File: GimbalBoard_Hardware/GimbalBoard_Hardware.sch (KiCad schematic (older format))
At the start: 3 parts

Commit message: added zenner diodes
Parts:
- added D1, D2: D_Zener, symbol Device:D_Zener
- gave numbers to parts that had none: 1
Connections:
- wire segments 26 -> 36
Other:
- note added: "Buck Converters"
- note added: "Power Input"
- moved on the sheet: Conn1A, Conn1B, Conn1C

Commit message: added servo indicator sheet and some connection
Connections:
- net labels removed: Servo_1_PWM, Servo_2_PWM, Servo_3_PWM, Servo_4_PWM, Servo_5_PWM, Servo_6_PWM, Servo_7_PWM, Servo_8_PWM
- wire segments 36 -> 37
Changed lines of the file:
@@
 $Descr A4 11693 8268
 encoding utf-8
-Sheet 1 6
+Sheet 1 7
 Title ""
 Date ""
@@
 Wire Wire Line
 	10000 1750 10250 1750
-Text GLabel 6050 4000 0    50   Output ~ 0
+Text GLabel 4850 900  0    50   Output ~ 0
 Servo_1_SW
 Wire Wire Line
-	6050 4000 6200 4000
-Text GLabel 6050 4150 0    50   Output ~ 0
+	4850 900  5000 900
+Text GLabel 4850 1050 0    50   Output ~ 0
 Servo_2_SW
 Wire Wire Line
-	6050 4150 6200 4150
-Text GLabel 6050 4300 0    50   Output ~ 0
+	4850 1050 5000 1050
+Text GLabel 4850 1200 0    50   Output ~ 0
 Servo_3_SW
 Wire Wire Line
-	6050 4300 6200 4300
-Text GLabel 6050 4450 0    50   Output ~ 0
+	4850 1200 5000 1200
+Text GLabel 4850 1350 0    50   Output ~ 0
 Servo_4_SW
 Wire Wire Line
-	6050 4450 6200 4450
-Text GLabel 6050 4600 0    50   Output ~ 0
+	4850 1350 5000 1350
+Text GLabel 4850 1500 0    50   Output ~ 0
 Servo_5_SW
 Wire Wire Line
-	6050 4600 6200 4600
-Text GLabel 6050 4750 0    50   Output ~ 0
+	4850 1500 5000 1500
+Text GLabel 4850 1650 0    50   Output ~ 0
 Servo_6_SW
 Wire Wire Line
-	6050 4750 6200 4750
-Text GLabel 6050 4900 0    50   Output ~ 0
+	4850 1650 5000 1650
+Text GLabel 4850 1800 0    50   Output ~ 0
 Servo_7_SW
 Wire Wire Line
-	6050 4900 6200 4900
-Text GLabel 6050 5050 0    50   Output ~ 0
+	4850 1800 5000 1800
+Text GLabel 4850 1950 0    50   Output ~ 0
 Servo_8_SW
 Wire Wire Line
-	6050 5050 6200 5050
-Text GLabel 7500 5400 2    50   Output ~ 0
+	4850 1950 5000 1950
+Text GLabel 6300 2300 2    50   Output ~ 0
 Servo_Digital_Control
 Wire Wire Line
-	7500 5400 7350 5400
-Text GLabel 7500 5550 2    50   Output ~ 0
+	6300 2300 6150 2300
+Text GLabel 6300 2450 2    50   Output ~ 0
 Servo_Manual_Control_Left
 Wire Wire Line
-	7500 5550 7350 5550
-Text GLabel 7500 5700 2    50   Output ~ 0
+	6300 2450 6150 2450
+Text GLabel 6300 2600 2    50   Output ~ 0
 Servo_Manual_Control_Right
 Wire Wire Line
-	7500 5700 7350 5700
-$Sheet
-S 9050 3800 1300 2250
+	6300 2600 6150 2600
+$Sheet
+S 9050 3800 1000 1700
 U 615E206C
 F0 "Molex" 50
@@
 F9 "Servo_7_PWM" I L 9050 5000 50
 F10 "Servo_8_PWM" I L 9050 5150 50
-$EndSheet
-Text GLabel 8900 4100 0    50   Input ~ 0
-Servo_1_PWM
-Text GLabel 8900 4250 0    50   Input ~ 0
-Servo_2_PWM
-Text GLabel 8900 4400 0    50   Input ~ 0
-Servo_3_PWM
-Text GLabel 8900 4550 0    50   Input ~ 0
-Servo_4_PWM
-Text GLabel 8900 4850 0    50   Input ~ 0
-Servo_6_PWM
-Text GLabel 8900 4700 0    50   Input ~ 0
-Servo_5_PWM
-Text GLabel 8900 5000 0    50   Input ~ 0
-Servo_7_PWM
-Text GLabel 8900 5150 0    50   Input ~ 0
-Servo_8_PWM
-Wire Wire Line
-	9050 4100 8900 4100
-Wire Wire Line
-	9050 4250 8900 4250
-Wire Wire Line
-	9050 4400 8900 4400
-Wire Wire Line
-	9050 4550 8900 4550
-Wire Wire Line
-	9050 4700 8900 4700
-Wire Wire Line
-	9050 4850 8900 4850
-Wire Wire Line
-	9050 5000 8900 5000
-Wire Wire Line
-	9050 5150 8900 5150
-Wire Wire Line
-	9050 3950 8750 3950
-$Comp
-L power:+5V #PWR?
-U 1 1 615FF71F
-P 8750 3950
-F 0 "#PWR?" H 8750 3800 50  0001 C CNN
-F 1 "+5V" V 8765 4078 50  0000 L CNN
-F 2 "" H 8750 3950 50  0001 C CNN
-F 3 "" H 8750 3950 50  0001 C CNN
-	1    8750 3950
-	0    -1   -1   0
-$EndComp
+F11 "GND" I L 9050 5300 50
+$EndSheet
 $Sheet
 S 2100 1850 1150 200
@@
 $EndComp
 $Sheet
-S 6200 3800 1150 2200
+S 5000 700  1150 2200
 U 615E1D59
 F0 "switches" 50
 F1 "switches.sch" 50
-F2 "Servo_1_SW" O L 6200 4000 50
-F3 "Servo_2_SW" O L 6200 4150 50
-F4 "Servo_3­_SW" O L 6200 4300 50
-F5 "Servo_4_SW" O L 6200 4450 50
-F6 "Servo_5_SW" O L 6200 4600 50
-F7 "Servo_6_SW" O L 6200 4750 50
-F8 "Servo_7_SW" O L 6200 4900 50
-F9 "Servo_8_SW" O L 6200 5050 50
-F10 "Servo_Digital_Control" O R 7350 5400 50
-F11 "Servo_Manual_Control_Left" O R 7350 5550 50
-F12 "Servo_Manual_Control_Right" O R 7350 5700 50
+F2 "Servo_1_SW" O L 5000 900 50
+F3 "Servo_2_SW" O L 5000 1050 50
+F4 "Servo_3­_SW" O L 5000 1200 50
+F5 "Servo_4_SW" O L 5000 1350 50
+F6 "Servo_5_SW" O L 5000 1500 50
+F7 "Servo_6_SW" O L 5000 1650 50
+F8 "Servo_7_SW" O L 5000 1800 50
+F9 "Servo_8_SW" O L 5000 1950 50
+F10 "Servo_Digital_Control" O R 6150 2300 50
+F11 "Servo_Manual_Control_Left" O R 6150 2450 50
+F12 "Servo_Manual_Control_Right" O R 6150 2600 50
 $EndSheet
 Wire Wire Line
@@
 Text Notes 2050 850  0    79   ~ 0
 Buck Converters
+$Sheet
+S 6550 3800 900  1600
+U 6162A3B9
+F0 "Servo Indicators" 79
+F1 "servo-indicators.sch" 79
+F2 "Servo_1_PWM" I R 7450 4100 50
+F3 "Servo_2_PWM" I R 7450 4250 50
+F4 "Servo_3_PWM" I R 7450 4400 50
+F5 "Servo_4_PWM" I R 7450 4550 50
+F6 "Servo_5_PWM" I R 7450 4700 50
+F7 "Servo_6_PWM" I R 7450 4850 50
+F8 "Servo_7_PWM" I R 7450 5000 50
+F9 "Servo_8_PWM" I R 7450 5150 50
+F10 "+5V" I R 7450 3950 50
+F11 "GND" I R 7450 5300 50
+$EndSheet
+Wire Wire Line
+	7450 4100 9050 4100
+Wire Wire Line
+	7450 4250 9050 4250
+Wire Wire Line
+	7450 4400 9050 4400
+Wire Wire Line
+	7450 4550 9050 4550
+Wire Wire Line
+	7450 4700 9050 4700
+Wire Wire Line
+	7450 4850 9050 4850
+Wire Wire Line
+	7450 5000 9050 5000
+Wire Wire Line
+	7450 5150 9050 5150
+Wire Wire Line
+	7450 3950 9050 3950
+Wire Wire Line
+	7450 5300 9050 5300
 $EndSCHEMATC

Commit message: power indicators
added power indicators
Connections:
- net labels removed: +12L, +12VA, +3.3V, +5V
- wire segments 37 -> 33
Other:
- note added: "+12VA\n"
- note added: "+12VL"
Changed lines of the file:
@@
 	1    0    0    -1
 $EndComp
-$Comp
-L power:+12VA #PWR?
-U 1 1 6160149D
-P 8550 1600
-F 0 "#PWR?" H 8550 1450 50  0001 C CNN
-F 1 "+12VA" V 8565 1727 50  0000 L CNN
-F 2 "" H 8550 1600 50  0001 C CNN
-F 3 "" H 8550 1600 50  0001 C CNN
-	1    8550 1600
-	0    -1   -1   0
-$EndComp
-$Comp
-L power:+12L #PWR?
-U 1 1 61602174
-P 8550 1750
-F 0 "#PWR?" H 8550 1600 50  0001 C CNN
-F 1 "+12L" V 8565 1878 50  0000 L CNN
-F 2 "" H 8550 1750 50  0001 C CNN
-F 3 "" H 8550 1750 50  0001 C CNN
-	1    8550 1750
-	0    -1   -1   0
-$EndComp
-$Comp
-L power:+5V #PWR?
-U 1 1 61602E2C
-P 10250 1600
-F 0 "#PWR?" H 10250 1450 50  0001 C CNN
-F 1 "+5V" V 10265 1728 50  0000 L CNN
-F 2 "" H 10250 1600 50  0001 C CNN
-F 3 "" H 10250 1600 50  0001 C CNN
-	1    10250 1600
-	0    1    1    0
-$EndComp
-$Comp
-L power:+3.3V #PWR?
-U 1 1 6160329C
-P 10250 1750
-F 0 "#PWR?" H 10250 1600 50  0001 C CNN
-F 1 "+3.3V" V 10265 1878 50  0000 L CNN
-F 2 "" H 10250 1750 50  0001 C CNN
-F 3 "" H 10250 1750 50  0001 C CNN
-	1    10250 1750
-	0    1    1    0
-$EndComp
-Wire Wire Line
-	8550 1600 8800 1600
-Wire Wire Line
-	8550 1750 8800 1750
-Wire Wire Line
-	10000 1600 10250 1600
-Wire Wire Line
-	10000 1750 10250 1750
 Text GLabel 4850 900  0    50   Output ~ 0
 Servo_1_SW
@@
 F2 "Power_Input_Act" I L 2100 1350 50
 F3 "+5V" I R 3250 1350 50
-$EndSheet
-$Sheet
-S 8800 1450 1200 500
-U 615B83A4
-F0 "Buck Converters" 50
-F1 "buck_converters.sch" 50
-F2 "Power_Input_Act" I L 8800 1600 50
-F3 "Power_Input_Log" I L 8800 1750 50
-F4 "+5V" I R 10000 1600 50
-F5 "+3.3V" I R 10000 1750 50
 $EndSheet
 $Comp
@@
 Wire Wire Line
 	7450 5300 9050 5300
+Text Notes 950  2050 0    50   ~ 0
++12VL
+Text Notes 950  1450 0    50   ~ 0
++12VA\n
+$Sheet
+S 2550 2500 750  650
+U 61616981
+F0 "Power_Indicators" 50
+F1 "Power_Indicators.sch" 50
+F2 "Power_Input_Act" I L 2550 2600 50
+F3 "Power_Input_Log" I L 2550 2750 50
+F4 "+5V" I L 2550 2900 50
+F5 "+3.3V" I L 2550 3050 50
+$EndSheet
 $EndSCHEMATC

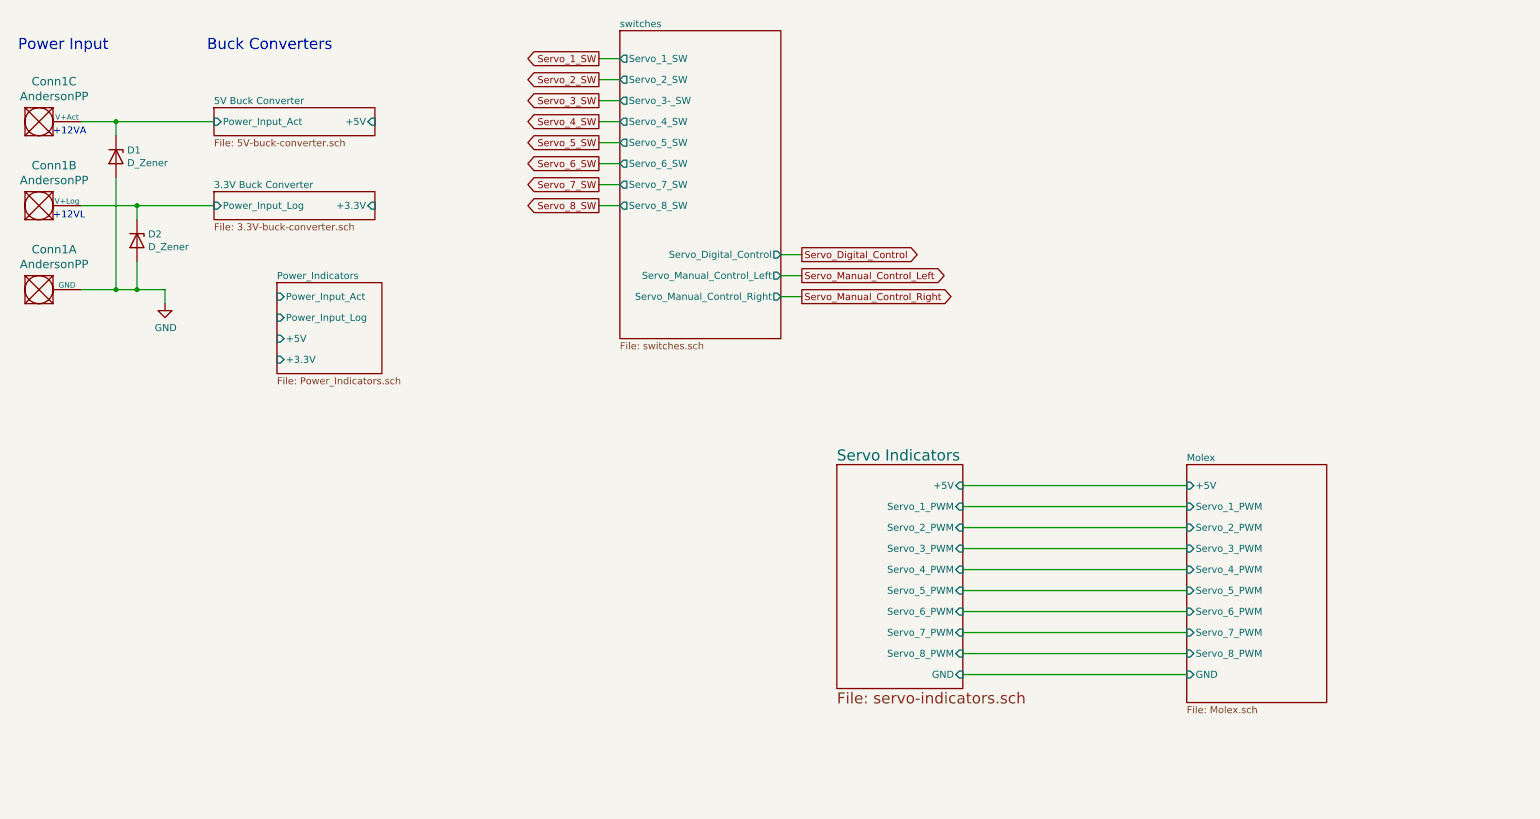
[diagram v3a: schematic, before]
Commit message: Added the Teensy
Added the Teensey and some tags and things. It should be done. or at least ready for review
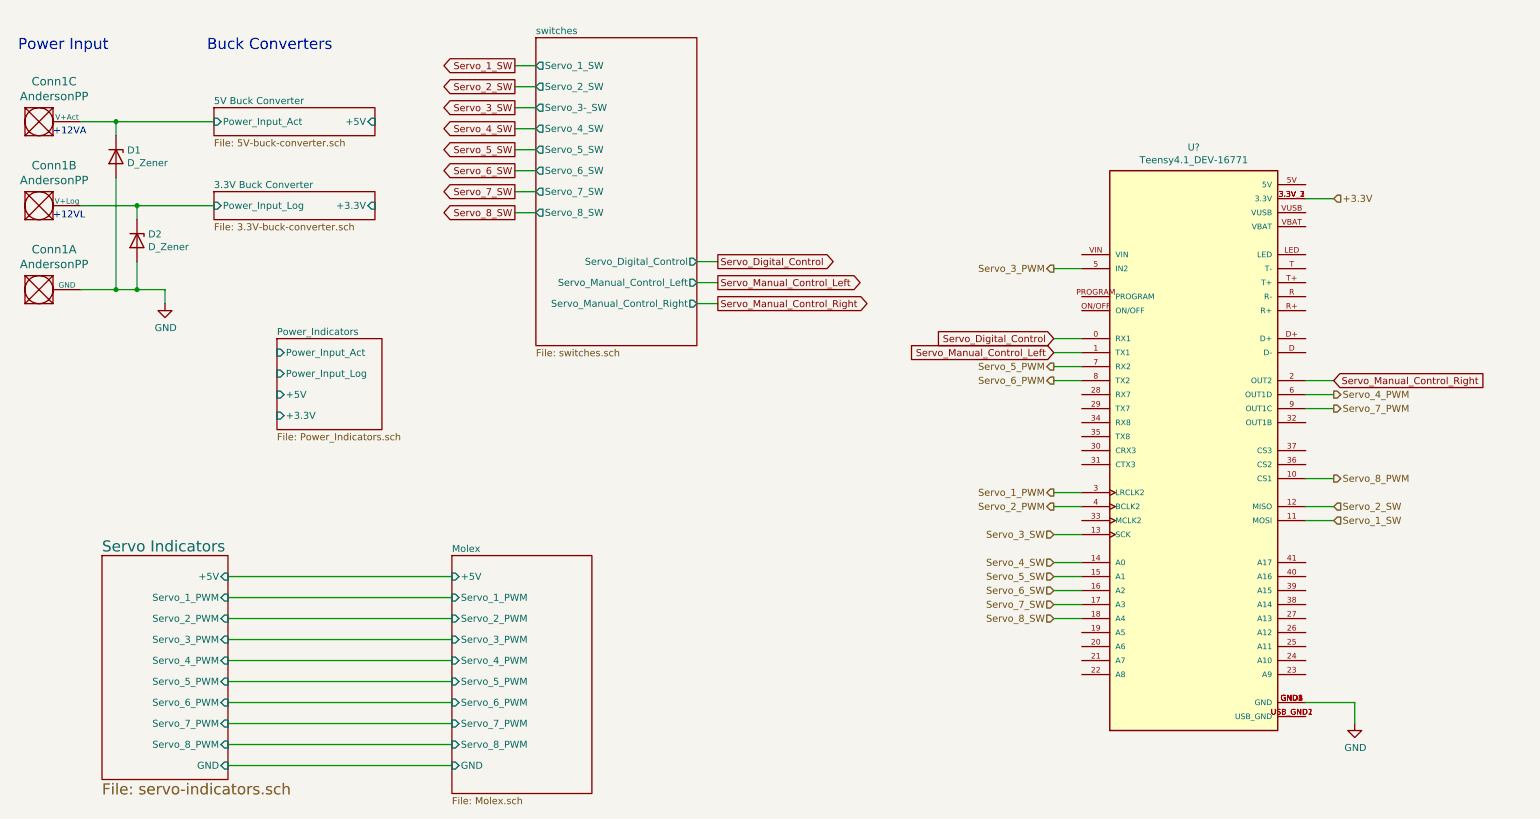
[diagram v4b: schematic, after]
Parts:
- added U?: Teensy4.1_DEV-16771, MODULE_DEV-16771, symbol MRDT_Shields:Teensy4.1_DEV-16771
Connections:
- net GND: now also U?.GND1 (GND), U?.GND2 (GND), U?.GND3 (GND), U?.GND4 (GND), U?.GND5 (GND)
- net Servo_1_SW: now also U?.11 (MOSI)
- net Servo_2_SW: now also U?.12 (MISO)
- net Servo_3_SW: now also U?.13 (SCK)
- net Servo_4_SW: now also U?.14 (A0)
- net Servo_5_SW: now also U?.15 (A1)
- net Servo_6_SW: now also U?.16 (A2)
- net Servo_7_SW: now also U?.17 (A3)
- net Servo_8_SW: now also U?.18 (A4)
- net Servo_Digital_Control: now also U?.0 (RX1)
- net Servo_Manual_Control_Left: now also U?.1 (TX1)
- net Servo_Manual_Control_Right: now also U?.2 (OUT2)
- new net: U?.USB_GND1 (USB_GND), U?.USB_GND2 (USB_GND)
- new net +3.3V: U?.3.3V_1 (3.3V), U?.3.3V_2 (3.3V), U?.3.3V_3 (3.3V)
- new net Servo_1_PWM: U?.3 (LRCLK2)
- new net Servo_2_PWM: U?.4 (BCLK2)
- new net Servo_3_PWM: U?.5 (IN2)
- new net Servo_4_PWM: U?.6 (OUT1D)
- new net Servo_5_PWM: U?.7 (RX2)
- new net Servo_6_PWM: U?.8 (TX2)
- new net Servo_7_PWM: U?.9 (OUT1C)
- new net Servo_8_PWM: U?.10 (CS1)

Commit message: connected everything up and changed power to accomodate teensy instead of tiva
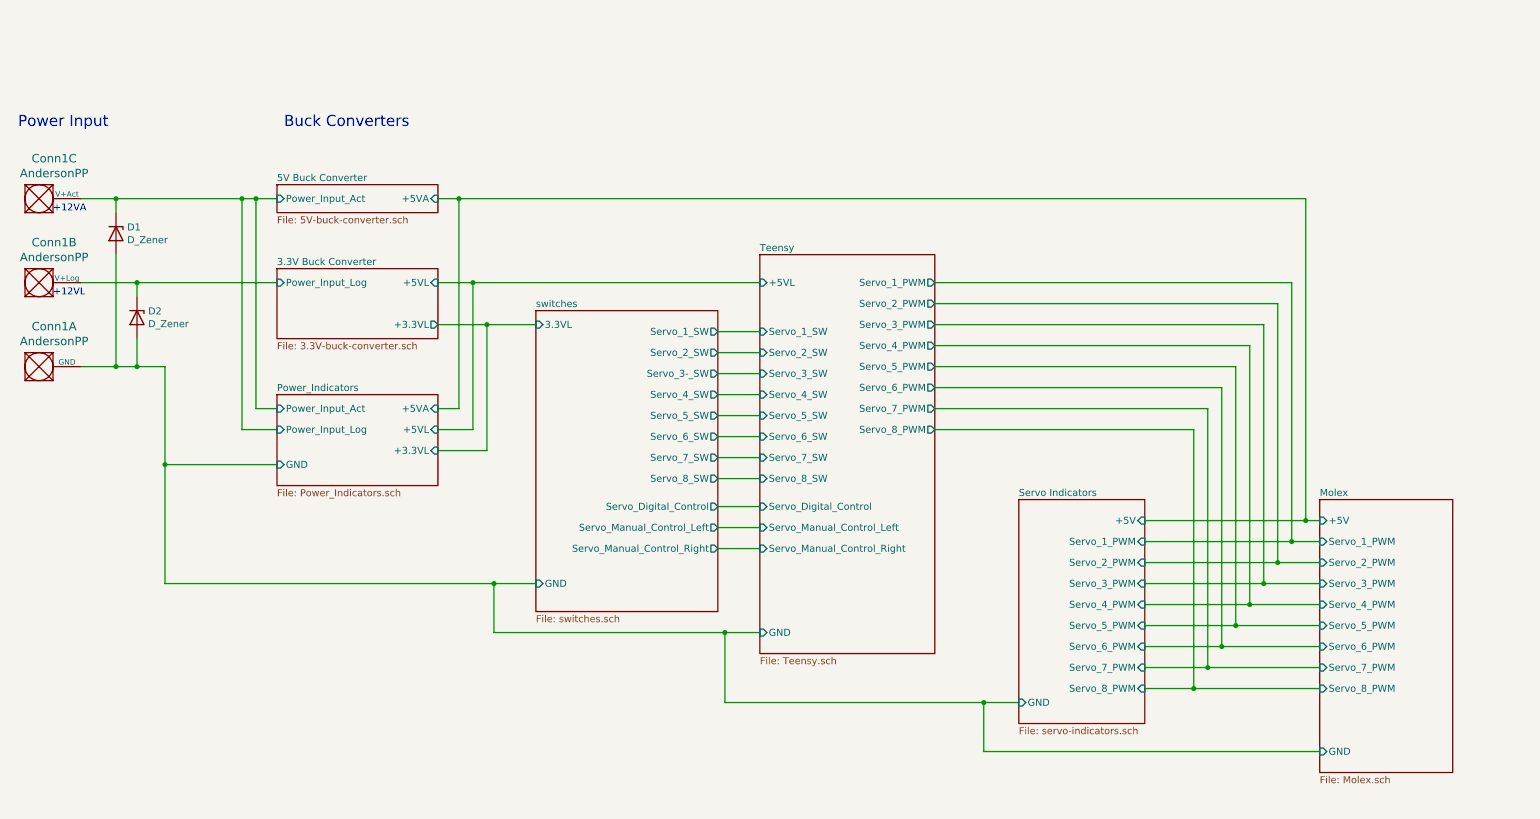
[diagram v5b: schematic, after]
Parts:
- removed U?: Teensy4.1_DEV-16771, MODULE_DEV-16771, symbol MRDT_Shields:Teensy4.1_DEV-16771
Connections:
- net GND is gone; now on net Molex/GND: Conn1.1 (GND), D1.2 (A), D2.2 (A)
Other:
- moved on the sheet: Conn1A, Conn1B, Conn1C, D1, D2

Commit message: added h-labels
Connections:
- net Molex/GND renamed 3.3V Buck Converter/GND
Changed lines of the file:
@@
 F3 "+5VL" I R 3700 2500 50
 F4 "+3.3VL" O R 3700 2800 50
-$EndSheet
-$Sheet
-S 2550 1800 1150 200
+F5 "GND" I L 2550 2800 50
+$EndSheet
+$Sheet
+S 2550 1800 1150 350
 U 61606E20
 F0 "5V Buck Converter" 50
@@
 F2 "Power_Input_Act" I L 2550 1900 50
 F3 "+5VA" I R 3700 1900 50
+F4 "GND" I L 2550 2050 50
 $EndSheet
 $Comp
@@
 Wire Wire Line
 	1550 2900 1550 3100
-Connection ~ 1550 3100
-Wire Wire Line
-	1550 3100 1750 3100
 Text Notes 700  1400 0    79   ~ 0
 Power Input
@@
 	9100 5400 10000 5400
 Wire Wire Line
-	1750 4650 4100 4650
-Wire Wire Line
-	1750 3100 1750 3800
-Wire Wire Line
 	4100 4650 4100 5000
 Wire Wire Line
 	4100 5000 5750 5000
-Connection ~ 4100 4650
 Wire Wire Line
 	4100 4650 4400 4650
@@
 	5700 4400 6000 4400
 Wire Wire Line
-	2550 3800 1750 3800
-Connection ~ 1750 3800
-Wire Wire Line
-	1750 3800 1750 4650
-Wire Wire Line
 	3850 1900 3850 3400
 Wire Wire Line
@@
 Wire Wire Line
 	2300 1900 2400 1900
+Wire Wire Line
+	2300 3800 2300 4650
+Wire Wire Line
+	2300 4650 4100 4650
+Wire Wire Line
+	2300 3800 2550 3800
+Connection ~ 4100 4650
+Wire Wire Line
+	1550 3100 1800 3100
+Wire Wire Line
+	2200 3100 2200 3800
+Connection ~ 1550 3100
+Wire Wire Line
+	2200 3800 2300 3800
+Connection ~ 2300 3800
+Wire Wire Line
+	2550 2050 1800 2050
+Wire Wire Line
+	1800 2050 1800 3100
+Connection ~ 1800 3100
+Wire Wire Line
+	1800 3100 1950 3100
+Wire Wire Line
+	2550 2800 1950 2800
+Wire Wire Line
+	1950 2800 1950 3100
+Connection ~ 1950 3100
+Wire Wire Line
+	1950 3100 2200 3100
 $EndSCHEMATC

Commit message: added text
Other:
- note added: "GND"
- note added: "Manual Switches"
- note added: "Microcontroller"
- note added: "Power Indicators"
- note added: "Servo Connectors\n"
- note added: "Servo Indicators"
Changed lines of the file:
@@
 Wire Wire Line
 	1550 2900 1550 3100
-Text Notes 700  1400 0    79   ~ 0
+Text Notes 650  1350 0    79   ~ 0
 Power Input
-Text Notes 2600 1400 0    79   ~ 0
+Text Notes 2600 1500 0    79   ~ 0
 Buck Converters
 Text Notes 950  2600 0    50   ~ 0
@@
 +12VA\n
 $Sheet
-S 2550 3300 1150 650
-U 61616981
-F0 "Power_Indicators" 50
-F1 "Power_Indicators.sch" 50
-F2 "Power_Input_Act" I L 2550 3400 50
-F3 "Power_Input_Log" I L 2550 3550 50
-F4 "+5VA" I R 3700 3400 50
-F5 "+5VL" I R 3700 3550 50
-F6 "+3.3VL" I R 3700 3700 50
-F7 "GND" I L 2550 3800 50
-$EndSheet
-$Sheet
 S 10000 4050 950  1950
 U 615E206C
@@
 F1 "Molex.sch" 50
 F2 "Servo_1_PWM" I L 10000 4350 50
-F3 "+5V" I L 10000 4200 50
-F4 "Servo_2_PWM" I L 10000 4500 50
-F5 "Servo_3_PWM" I L 10000 4650 50
-F6 "Servo_4_PWM" I L 10000 4800 50
-F7 "Servo_5_PWM" I L 10000 4950 50
-F8 "Servo_6_PWM" I L 10000 5100 50
-F9 "Servo_7_PWM" I L 10000 5250 50
-F10 "Servo_8_PWM" I L 10000 5400 50
-F11 "GND" I L 10000 5850 50
+F3 "Servo_2_PWM" I L 10000 4500 50
+F4 "Servo_3_PWM" I L 10000 4650 50
+F5 "Servo_4_PWM" I L 10000 4800 50
+F6 "Servo_5_PWM" I L 10000 4950 50
+F7 "Servo_6_PWM" I L 10000 5100 50
+F8 "Servo_7_PWM" I L 10000 5250 50
+F9 "Servo_8_PWM" I L 10000 5400 50
+F10 "GND" I L 10000 5850 50
+F11 "+5VA" I L 10000 4200 50
 $EndSheet
 $Sheet
@@
 F8 "Servo_7_PWM" I R 8750 5250 50
 F9 "Servo_8_PWM" I R 8750 5400 50
-F10 "+5V" I R 8750 4200 50
-F11 "GND" I L 7850 5500 50
+F10 "GND" I L 7850 5500 50
+F11 "+5VA" I R 8750 4200 50
 $EndSheet
 Wire Wire Line
@@
 Wire Wire Line
 	5700 4400 6000 4400
-Wire Wire Line
-	3850 1900 3850 3400
-Wire Wire Line
-	3850 3400 3700 3400
 Connection ~ 3850 1900
 Wire Wire Line
 	3850 1900 9900 1900
-Wire Wire Line
-	3950 2500 3950 3550
-Wire Wire Line
-	3950 3550 3700 3550
 Connection ~ 3950 2500
 Wire Wire Line
 	3950 2500 6000 2500
-Wire Wire Line
-	4050 2800 4050 3700
-Wire Wire Line
-	4050 3700 3700 3700
 Connection ~ 4050 2800
 Wire Wire Line
 	4050 2800 4400 2800
-Wire Wire Line
-	2550 3400 2400 3400
-Wire Wire Line
-	2400 3400 2400 1900
 Connection ~ 2400 1900
 Wire Wire Line
 	2400 1900 2550 1900
-Wire Wire Line
-	2550 3550 2300 3550
-Wire Wire Line
-	2300 3550 2300 1900
 Connection ~ 2300 1900
 Wire Wire Line
 	2300 1900 2400 1900
 Wire Wire Line
-	2300 3800 2300 4650
-Wire Wire Line
-	2300 4650 4100 4650
-Wire Wire Line
-	2300 3800 2550 3800
-Connection ~ 4100 4650
-Wire Wire Line
 	1550 3100 1800 3100
-Wire Wire Line
-	2200 3100 2200 3800
 Connection ~ 1550 3100
-Wire Wire Line
-	2200 3800 2300 3800
-Connection ~ 2300 3800
 Wire Wire Line
 	2550 2050 1800 2050
@@
 Wire Wire Line
 	1950 3100 2200 3100
+$Sheet
+S 2550 3650 1150 650
+U 61616981
+F0 "Power_Indicators" 50
+F1 "Power_Indicators.sch" 50
+F2 "Power_Input_Act" I L 2550 3750 50
+F3 "Power_Input_Log" I L 2550 3900 50
+F4 "+5VA" I R 3700 3750 50
+F5 "+5VL" I R 3700 3900 50
+F6 "+3.3VL" I R 3700 4050 50
+F7 "GND" I L 2550 4150 50
+$EndSheet
+Text Notes 950  3200 0    50   ~ 0
+GND
+Text Notes 4450 2300 0    79   ~ 0
+Manual Switches
+Text Notes 6050 1700 0    79   ~ 0
+Microcontroller
+Text Notes 7800 3800 0    79   ~ 0
+Servo Indicators
+Text Notes 10000 3800 0    79   ~ 0
+Servo Connectors\n
+Text Notes 2600 3350 0    79   ~ 0
+Power Indicators
+Wire Wire Line
+	2200 4150 2350 4150
+Wire Wire Line
+	2200 3100 2200 4150
+Wire Wire Line
+	2400 3750 2550 3750
+Wire Wire Line
+	2400 1900 2400 3750
+Wire Wire Line
+	2300 3900 2550 3900
+Wire Wire Line
+	2300 1900 2300 3900
+Wire Wire Line
+	3850 3750 3700 3750
+Wire Wire Line
+	3850 1900 3850 3750
+Wire Wire Line
+	3950 3900 3700 3900
+Wire Wire Line
+	3950 2500 3950 3900
+Wire Wire Line
+	4050 4050 3700 4050
+Wire Wire Line
+	4050 2800 4050 4050
+Wire Wire Line
+	4100 4650 2350 4650
+Wire Wire Line
+	2350 4650 2350 4150
+Connection ~ 4100 4650
+Connection ~ 2350 4150
+Wire Wire Line
+	2350 4150 2550 4150
 $EndSCHEMATC
